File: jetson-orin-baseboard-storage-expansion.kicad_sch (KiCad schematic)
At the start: 0 parts

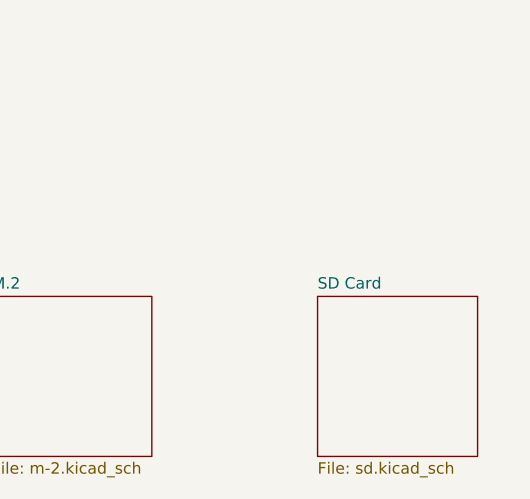
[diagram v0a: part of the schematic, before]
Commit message: [#64333] Continued routing components
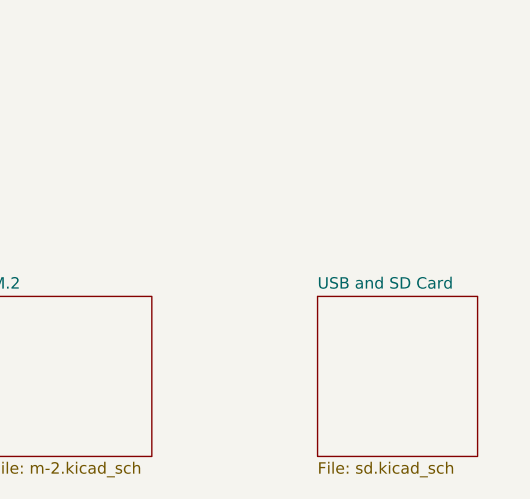
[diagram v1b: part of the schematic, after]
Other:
- sheet SD Card renamed USB and SD Card
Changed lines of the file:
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@@
     (stroke (width 0.1524) (type solid))
     (fill (color 0 0 0 0.0000))
-    (property "Sheetname" "SD Card" (at 241.935 131.3684 0)
+    (property "Sheetname" "USB and SD Card" (at 241.935 131.3684 0)
       (effects (font (size 1.27 1.27)) (justify left bottom))
     )
